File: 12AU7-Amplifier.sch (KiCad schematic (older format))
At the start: 33 parts, among them J1 SJ1-3523N, J2 Barrel_Jack, J3 SJ1-3523N, Q1 IRF510, Q2 IRF510, SW1 100SP1T2B4M7QE, U1 12AU7, U2 LM317, U3 LM317

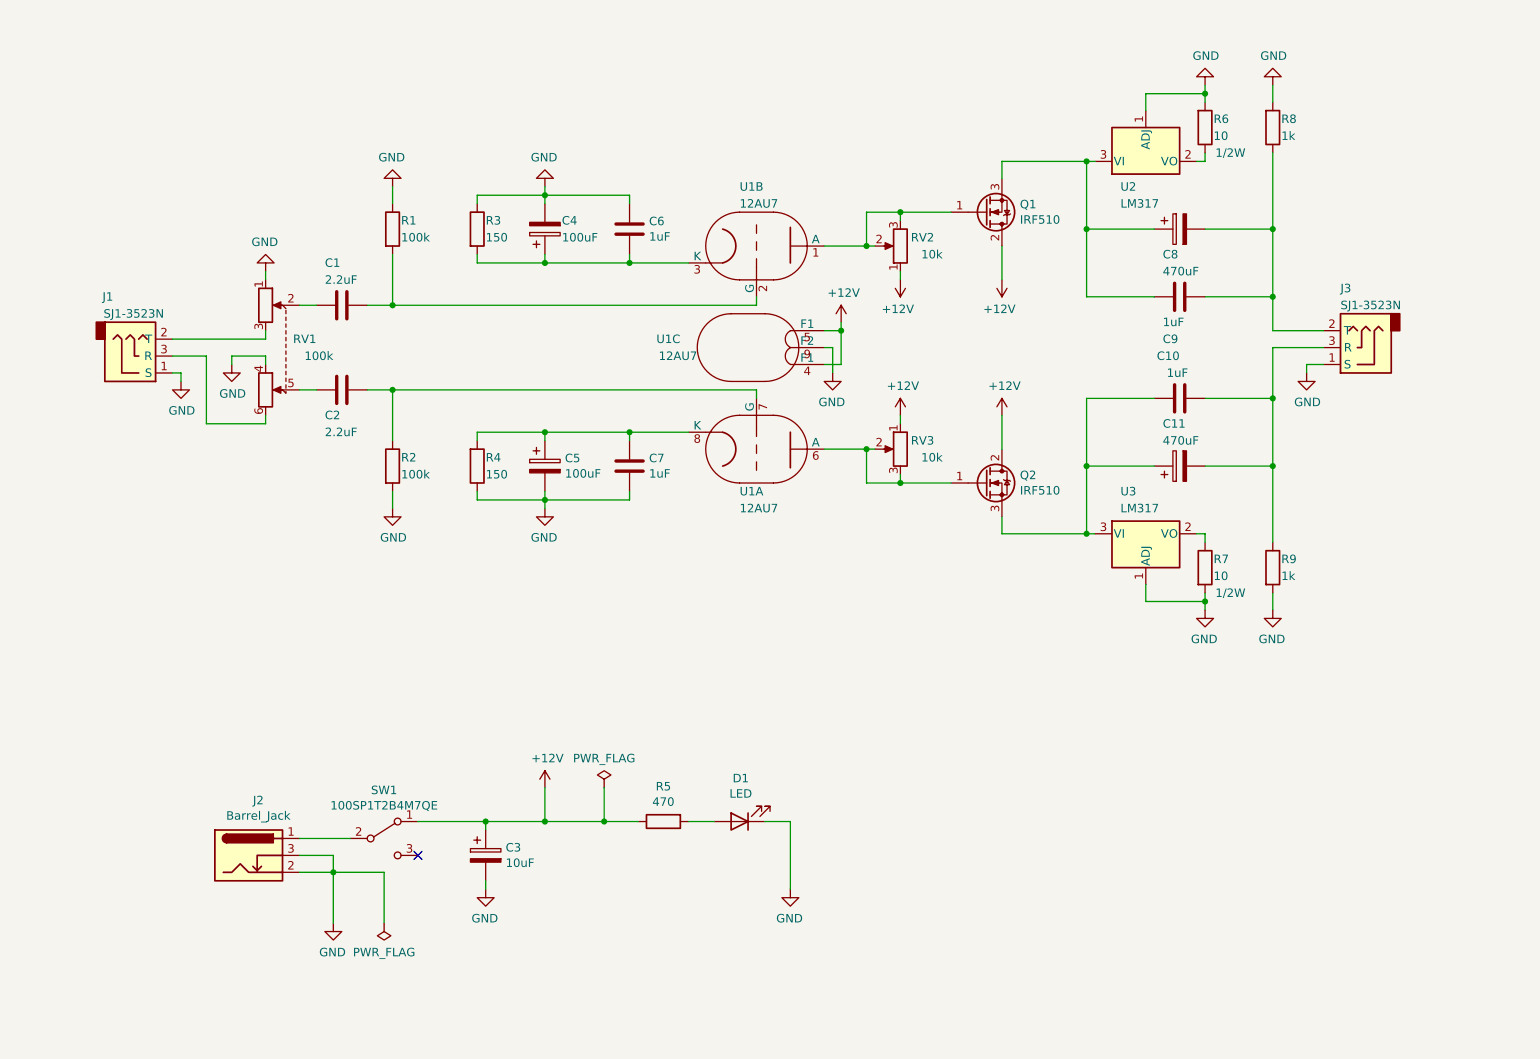
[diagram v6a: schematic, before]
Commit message: Component layout for Hammond case
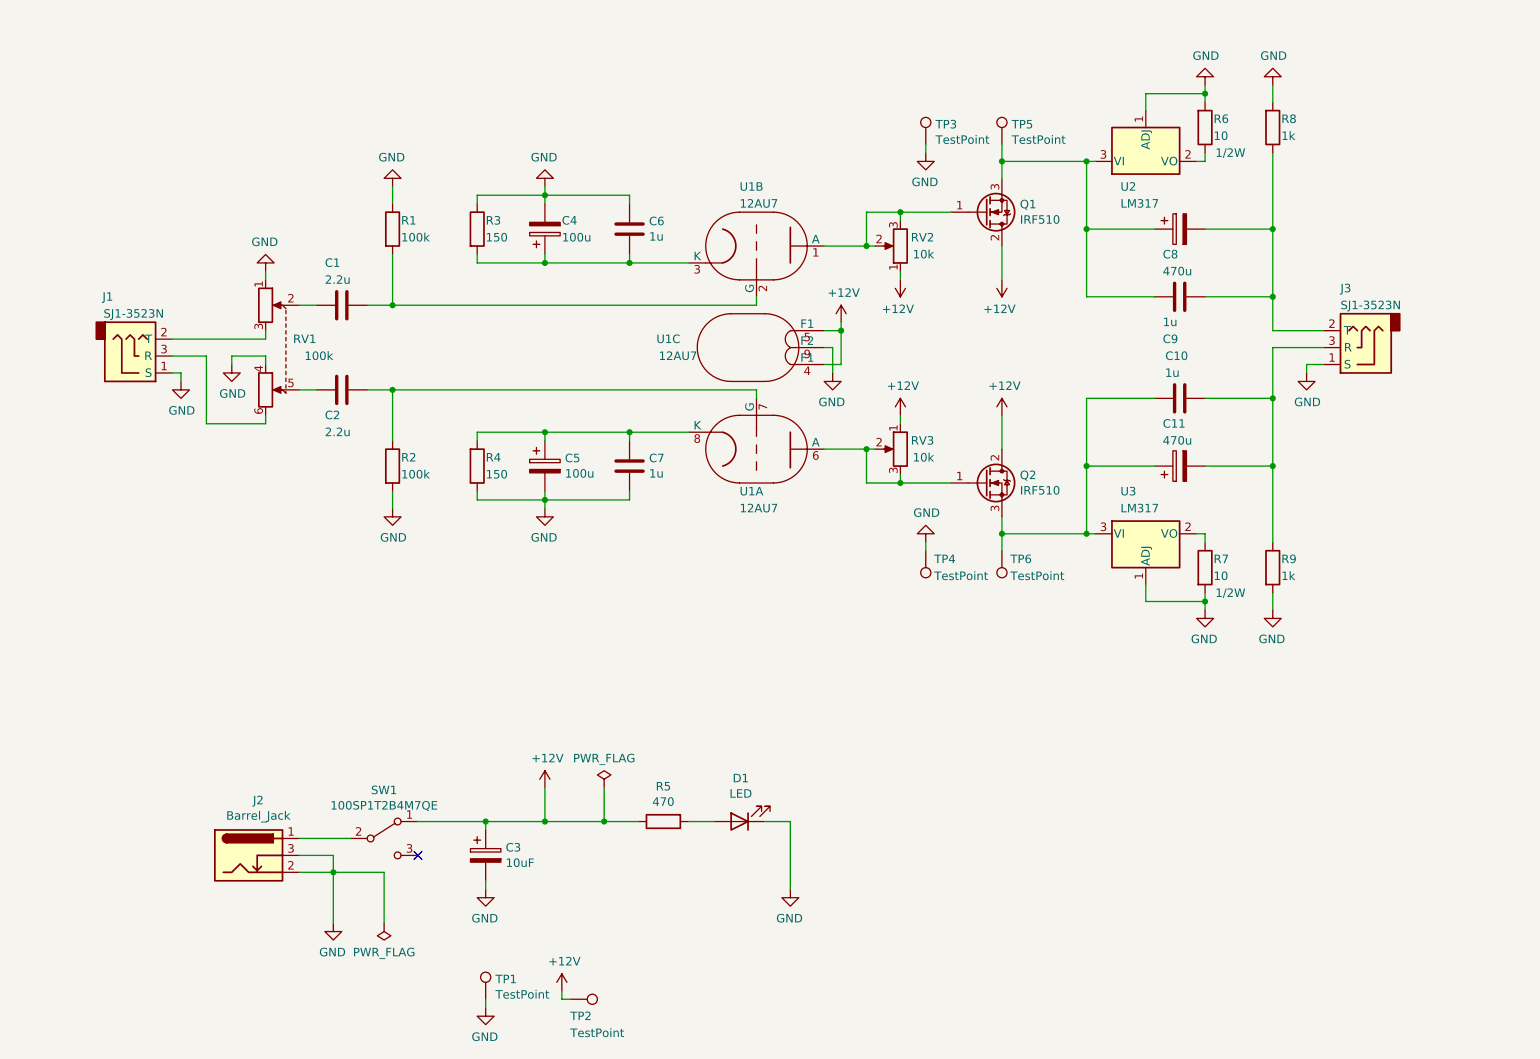
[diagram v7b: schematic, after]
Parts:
- added TP1, TP3, TP4: TestPoint, TestPoint:TestPoint_THTPad_2.0x2.0mm_Drill1.0mm, symbol Connector:TestPoint
- added TP2, TP5, TP6: TestPoint, TestPoint:TestPoint_THTPad_D2.0mm_Drill1.0mm, symbol Connector:TestPoint
- C1, C2: value 2.2uF -> 2.2u
- C10, C6, C7, C9: value 1uF -> 1u
- C11, C8: value 470uF -> 470u
- C4, C5: value 100uF -> 100u
- R3, R4: footprint Resistor_THT:R_Axial_DIN0614_L14.3mm_D5.7mm_P5.08mm_Vertical -> Resistor_THT:R_Axial_DIN0207_L6.3mm_D2.5mm_P10.16mm_Horizontal
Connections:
- net +12V: now also TP2.1
- net GND: now also TP1.1, TP3.1, TP4.1
- net at C10.1, C11.1, Q2.3 (S)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: now also TP6.1
- net at C8.1, C9.2, Q1.3 (S)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: now also TP5.1
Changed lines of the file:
@@
 P 7850 2500
 F 0 "C8" V 8000 2600 50  0000 R CNN
-F 1 "470uF" V 8100 2600 50  0000 R CNN
+F 1 "470u" V 8100 2600 50  0000 R CNN
 F 2 "Capacitor_THT:CP_Radial_D10.0mm_P5.00mm" H 7888 2350 50  0001 C CNN
 F 3 "~" H 7850 2500 50  0001 C CNN
@@
 P 6200 2600
 F 0 "RV2" H 6000 2550 50  0000 L CNN
-F 1 "10k" H 5950 2650 50  0000 L CNN
+F 1 "10k" H 6000 2650 50  0000 L CNN
 F 2 "12AU7-Amplifier:CT6EP103" H 6200 2600 50  0001 C CNN
 F 3 "~" H 6200 2600 50  0001 C CNN
@@
 P 2900 3450
 F 0 "C2" V 3050 3350 50  0000 L CNN
-F 1 "2.2uF" V 3150 3350 50  0000 L CNN
+F 1 "2.2u" V 3150 3350 50  0000 L CNN
 F 2 "Capacitor_THT:C_Rect_L18.0mm_W11.0mm_P15.00mm_FKS3_FKP3" H 2938 3300 50  0001 C CNN
 F 3 "https://b2b-api.panasonic.eu/file_stream/pids/fileversion/998" H 2900 3450 50  0001 C CNN
@@
 P 2900 2950
 F 0 "C1" V 3150 2850 50  0000 L CNN
-F 1 "2.2uF" V 3050 2850 50  0000 L CNN
+F 1 "2.2u" V 3050 2850 50  0000 L CNN
 F 2 "Capacitor_THT:C_Rect_L18.0mm_W11.0mm_P15.00mm_FKS3_FKP3" H 2938 2800 50  0001 C CNN
 F 3 "https://b2b-api.panasonic.eu/file_stream/pids/fileversion/998" H 2900 2950 50  0001 C CNN
@@
 P 4100 3900
 F 0 "C5" H 4218 3946 50  0000 L CNN
-F 1 "100uF" H 4218 3855 50  0000 L CNN
+F 1 "100u" H 4218 3855 50  0000 L CNN
 F 2 "Capacitor_THT:CP_Radial_D8.0mm_P3.50mm" H 4138 3750 50  0001 C CNN
 F 3 "~" H 4100 3900 50  0001 C CNN
@@
 P 4100 2500
 F 0 "C4" H 4200 2450 50  0000 L CNN
-F 1 "100uF" H 4200 2550 50  0000 L CNN
+F 1 "100u" H 4200 2550 50  0000 L CNN
 F 2 "Capacitor_THT:CP_Radial_D8.0mm_P3.50mm" H 4138 2350 50  0001 C CNN
 F 3 "~" H 4100 2500 50  0001 C CNN
@@
 P 6200 3800
 F 0 "RV3" H 6000 3850 50  0000 L CNN
-F 1 "10k" H 5950 3750 50  0000 L CNN
+F 1 "10k" H 6000 3750 50  0000 L CNN
 F 2 "12AU7-Amplifier:CT6EP103" H 6200 3800 50  0001 C CNN
 F 3 "~" H 6200 3800 50  0001 C CNN
@@
 F 0 "R4" H 3750 3850 50  0000 L CNN
 F 1 "150" H 3750 3950 50  0000 L CNN
-F 2 "Resistor_THT:R_Axial_DIN0614_L14.3mm_D5.7mm_P5.08mm_Vertical" V 3630 3900 50  0001 C CNN
+F 2 "Resistor_THT:R_Axial_DIN0207_L6.3mm_D2.5mm_P10.16mm_Horizontal" V 3630 3900 50  0001 C CNN
 F 3 "~" H 3700 3900 50  0001 C CNN
 	1    3700 3900
@@
 F 0 "R3" H 3750 2550 50  0000 L CNN
 F 1 "150" H 3750 2450 50  0000 L CNN
-F 2 "Resistor_THT:R_Axial_DIN0614_L14.3mm_D5.7mm_P5.08mm_Vertical" V 3630 2500 50  0001 C CNN
+F 2 "Resistor_THT:R_Axial_DIN0207_L6.3mm_D2.5mm_P10.16mm_Horizontal" V 3630 2500 50  0001 C CNN
 F 3 "~" H 3700 2500 50  0001 C CNN
 	1    3700 2500
@@
 P 7850 3900
 F 0 "C11" V 8100 4000 50  0000 R CNN
-F 1 "470uF" V 8000 4000 50  0000 R CNN
+F 1 "470u" V 8000 4000 50  0000 R CNN
 F 2 "Capacitor_THT:CP_Radial_D10.0mm_P5.00mm" H 7888 3750 50  0001 C CNN
 F 3 "~" H 7850 3900 50  0001 C CNN
@@
 P 4600 2500
 F 0 "C6" H 4715 2546 50  0000 L CNN
-F 1 "1uF" H 4715 2455 50  0000 L CNN
+F 1 "1u" H 4715 2455 50  0000 L CNN
 F 2 "Capacitor_THT:C_Rect_L18.0mm_W8.0mm_P15.00mm_FKS3_FKP3" H 4638 2350 50  0001 C CNN
 F 3 "https://b2b-api.panasonic.eu/file_stream/pids/fileversion/998" H 4600 2500 50  0001 C CNN
@@
 P 4600 3900
 F 0 "C7" H 4715 3946 50  0000 L CNN
-F 1 "1uF" H 4715 3855 50  0000 L CNN
+F 1 "1u" H 4715 3855 50  0000 L CNN
 F 2 "Capacitor_THT:C_Rect_L18.0mm_W8.0mm_P15.00mm_FKS3_FKP3" H 4638 3750 50  0001 C CNN
 F 3 "https://b2b-api.panasonic.eu/file_stream/pids/fileversion/998" H 4600 3900 50  0001 C CNN
@@
 U 1 1 5FB4A0DE
 P 7850 3500
-F 0 "C10" V 8100 3500 50  0000 L CNN
-F 1 "1uF" V 8000 3450 50  0000 L CNN
+F 0 "C10" V 8100 3450 50  0000 L CNN
+F 1 "1u" V 8000 3500 50  0000 L CNN
 F 2 "Capacitor_THT:C_Rect_L18.0mm_W8.0mm_P15.00mm_FKS3_FKP3" H 7888 3350 50  0001 C CNN
 F 3 "https://b2b-api.panasonic.eu/file_stream/pids/fileversion/998" H 7850 3500 50  0001 C CNN
@@
 P 7850 2900
 F 0 "C9" V 8100 2800 50  0000 L CNN
-F 1 "1uF" V 8000 2800 50  0000 L CNN
+F 1 "1u" V 8000 2800 50  0000 L CNN
 F 2 "Capacitor_THT:C_Rect_L18.0mm_W8.0mm_P15.00mm_FKS3_FKP3" H 7888 2750 50  0001 C CNN
 F 3 "https://b2b-api.panasonic.eu/file_stream/pids/fileversion/998" H 7850 2900 50  0001 C CNN
@@
 	8400 3200 8700 3200
 Connection ~ 8400 3500
+$Comp
+L Connector:TestPoint TP5
+U 1 1 5FC3E929
+P 6800 2000
+F 0 "TP5" H 6858 2118 50  0000 L CNN
+F 1 "TestPoint" H 6858 2027 50  0000 L CNN
+F 2 "TestPoint:TestPoint_THTPad_D2.0mm_Drill1.0mm" H 7000 2000 50  0001 C CNN
+F 3 "~" H 7000 2000 50  0001 C CNN
+	1    6800 2000
+	1    0    0    -1
+$EndComp
+$Comp
+L Connector:TestPoint TP3
+U 1 1 5FC3F9B1
+P 6350 2000
+F 0 "TP3" H 6408 2118 50  0000 L CNN
+F 1 "TestPoint" H 6408 2027 50  0000 L CNN
+F 2 "TestPoint:TestPoint_THTPad_2.0x2.0mm_Drill1.0mm" H 6550 2000 50  0001 C CNN
+F 3 "~" H 6550 2000 50  0001 C CNN
+	1    6350 2000
+	1    0    0    -1
+$EndComp
+$Comp
+L power:GND #PWR025
+U 1 1 5FC531A8
+P 6350 2050
+F 0 "#PWR025" H 6350 1800 50  0001 C CNN
+F 1 "GND" H 6355 1877 50  0000 C CNN
+F 2 "" H 6350 2050 50  0001 C CNN
+F 3 "" H 6350 2050 50  0001 C CNN
+	1    6350 2050
+	-1   0    0    -1
+$EndComp
+Wire Wire Line
+	6350 2050 6350 2000
+$Comp
+L power:GND #PWR026
+U 1 1 5FCA6BAC
+P 6350 4350
+F 0 "#PWR026" H 6350 4100 50  0001 C CNN
+F 1 "GND" H 6355 4177 50  0000 C CNN
+F 2 "" H 6350 4350 50  0001 C CNN
+F 3 "" H 6350 4350 50  0001 C CNN
+	1    6350 4350
+	1    0    0    1
+$EndComp
+Wire Wire Line
+	6350 4400 6350 4350
+Wire Wire Line
+	6800 2100 6800 2000
+Connection ~ 6800 2100
+Wire Wire Line
+	6800 4400 6800 4300
+Connection ~ 6800 4300
+$Comp
+L Connector:TestPoint TP6
+U 1 1 5FC52447
+P 6800 4400
+F 0 "TP6" H 6750 4450 50  0000 R CNN
+F 1 "TestPoint" H 6750 4550 50  0000 R CNN
+F 2 "TestPoint:TestPoint_THTPad_D2.0mm_Drill1.0mm" H 7000 4400 50  0001 C CNN
+F 3 "~" H 7000 4400 50  0001 C CNN
+	1    6800 4400
+	-1   0    0    1
+$EndComp
+$Comp
+L Connector:TestPoint TP4
+U 1 1 5FD1CD23
+P 6350 4400
+F 0 "TP4" H 6300 4450 50  0000 R CNN
+F 1 "TestPoint" H 6300 4550 50  0000 R CNN
+F 2 "TestPoint:TestPoint_THTPad_2.0x2.0mm_Drill1.0mm" H 6550 4400 50  0001 C CNN
+F 3 "~" H 6550 4400 50  0001 C CNN
+	1    6350 4400
+	-1   0    0    1
+$EndComp
+$Comp
+L Connector:TestPoint TP1
+U 1 1 5FC3DDA6
+P 3750 7050
+F 0 "TP1" H 3808 7168 50  0000 L CNN
+F 1 "TestPoint" H 3808 7077 50  0000 L CNN
+F 2 "TestPoint:TestPoint_THTPad_2.0x2.0mm_Drill1.0mm" H 3950 7050 50  0001 C CNN
+F 3 "~" H 3950 7050 50  0001 C CNN
+	1    3750 7050
+	1    0    0    -1
+$EndComp
+$Comp
+L power:GND #PWR023
+U 1 1 5FD7B78E
+P 3750 7100
+F 0 "#PWR023" H 3750 6850 50  0001 C CNN
+F 1 "GND" H 3755 6927 50  0000 C CNN
+F 2 "" H 3750 7100 50  0001 C CNN
+F 3 "" H 3750 7100 50  0001 C CNN
+	1    3750 7100
+	-1   0    0    -1
+$EndComp
+Wire Wire Line
+	3750 7100 3750 7050
+$Comp
+L power:+12V #PWR024
+U 1 1 5FD818C1
+P 4200 7000
+F 0 "#PWR024" H 4200 6850 50  0001 C CNN
+F 1 "+12V" H 4215 7173 50  0000 C CNN
+F 2 "" H 4200 7000 50  0001 C CNN
+F 3 "" H 4200 7000 50  0001 C CNN
+	1    4200 7000
+	1    0    0    -1
+$EndComp
+$Comp
+L Connector:TestPoint TP2
+U 1 1 5FD879CC
+P 4250 7050
+F 0 "TP2" V 4350 7050 50  0000 L CNN
+F 1 "TestPoint" V 4450 7050 50  0000 L CNN
+F 2 "TestPoint:TestPoint_THTPad_D2.0mm_Drill1.0mm" H 4450 7050 50  0001 C CNN
+F 3 "~" H 4450 7050 50  0001 C CNN
+	1    4250 7050
+	0    1    1    0
+$EndComp
+Wire Wire Line
+	4200 7000 4200 7050
+Wire Wire Line
+	4200 7050 4250 7050
 $EndSCHEMATC
